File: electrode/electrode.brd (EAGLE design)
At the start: 36 x 39 mm, 17 parts, among them J1 FFC-32, U1 DG406DYZ-T, U2 DG406DYZ-T, U3 AD5933YRSZ

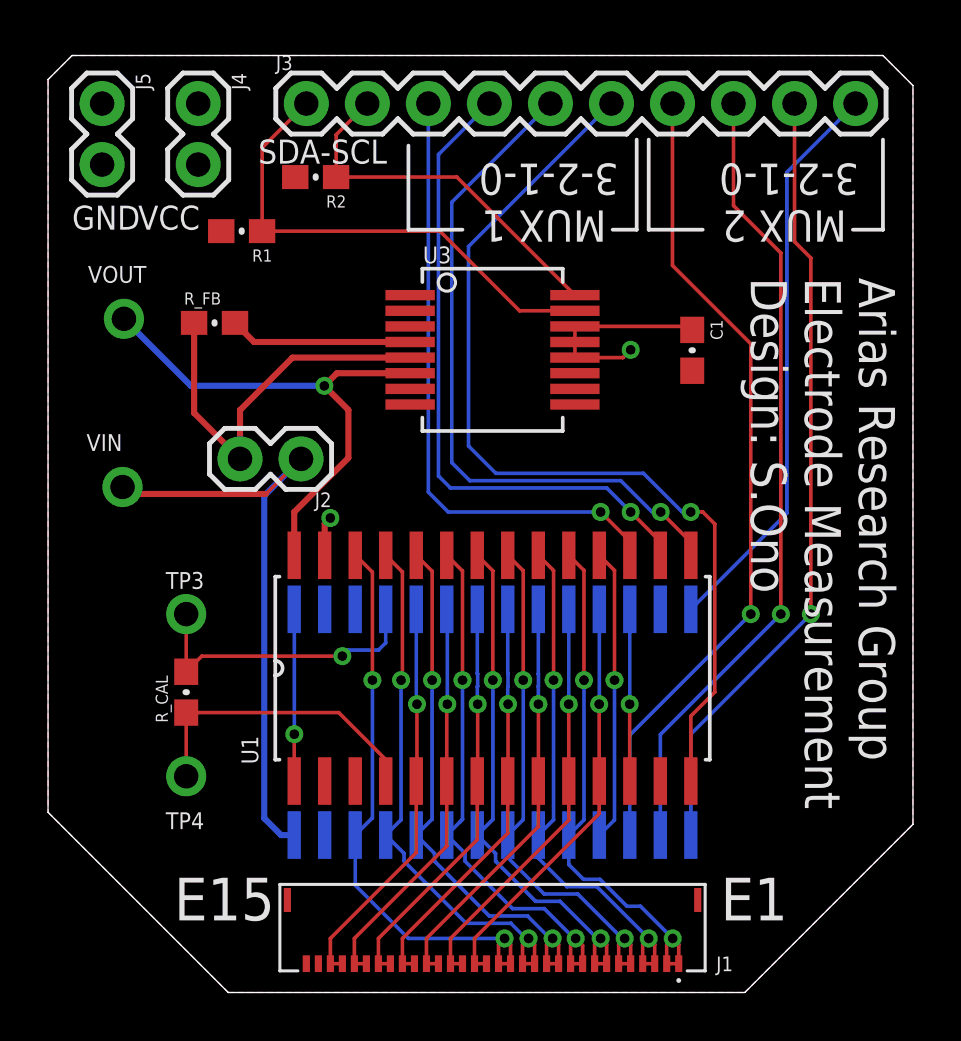
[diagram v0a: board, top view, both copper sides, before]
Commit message: send boards out for production and fix imp test code
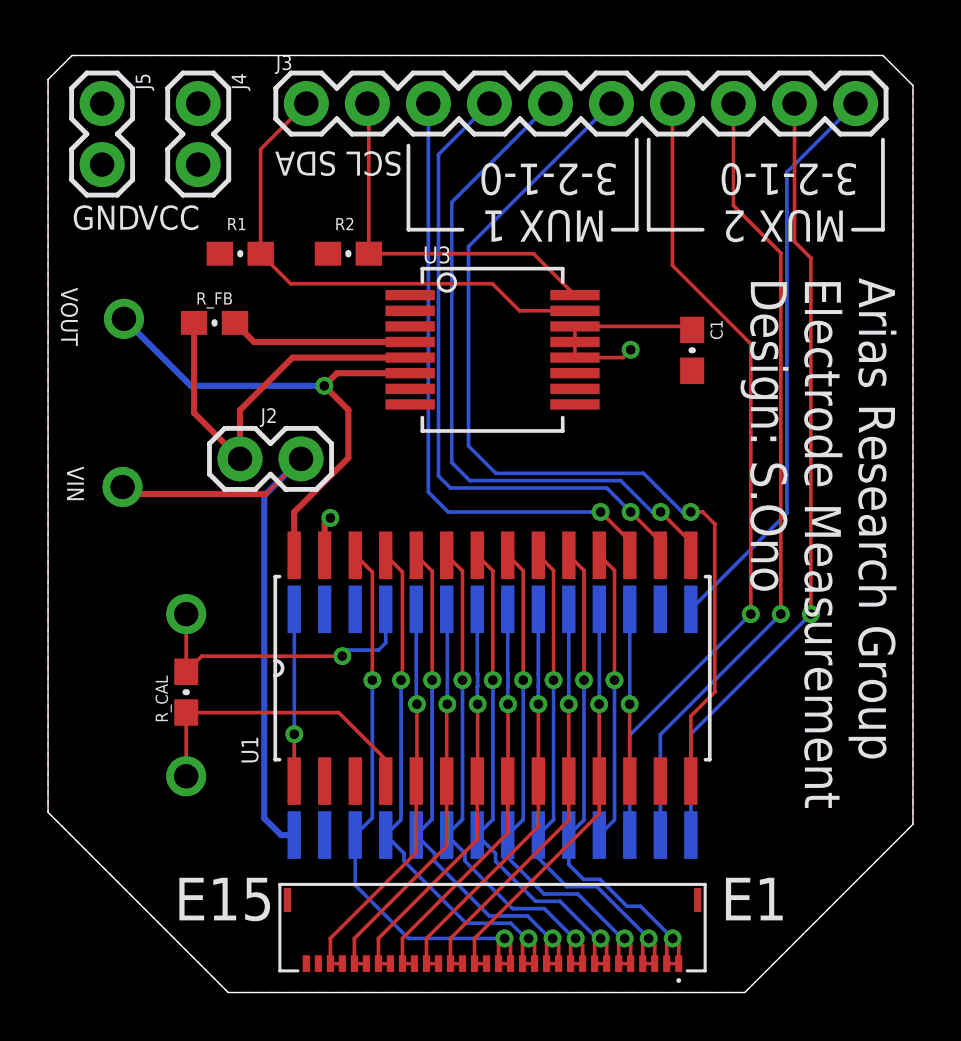
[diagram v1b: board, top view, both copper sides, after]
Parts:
- moved R2 3.47 mm to (16.0, 31.0)
- moved R1 0.94 mm to (11.5, 31.0)
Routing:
- net SDA: track 20.5 -> 21.1 mm
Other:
- board text added: "SCL SDA"
- board text removed: "SDA-SCL"
